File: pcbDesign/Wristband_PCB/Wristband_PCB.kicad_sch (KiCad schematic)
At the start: 5 parts, among them U1 module_adxl345, U2 SEN0344, U3 ESP32-C3_SUPERMINI_TH

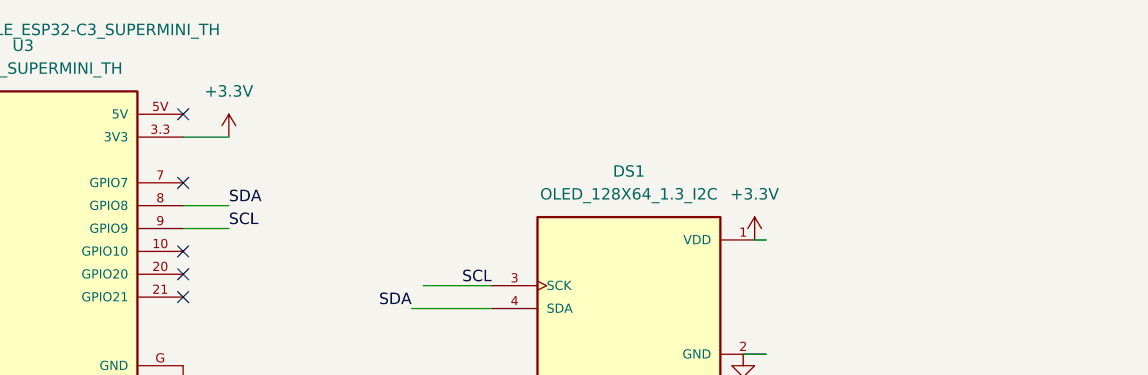
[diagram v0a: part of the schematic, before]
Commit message: added a power socket
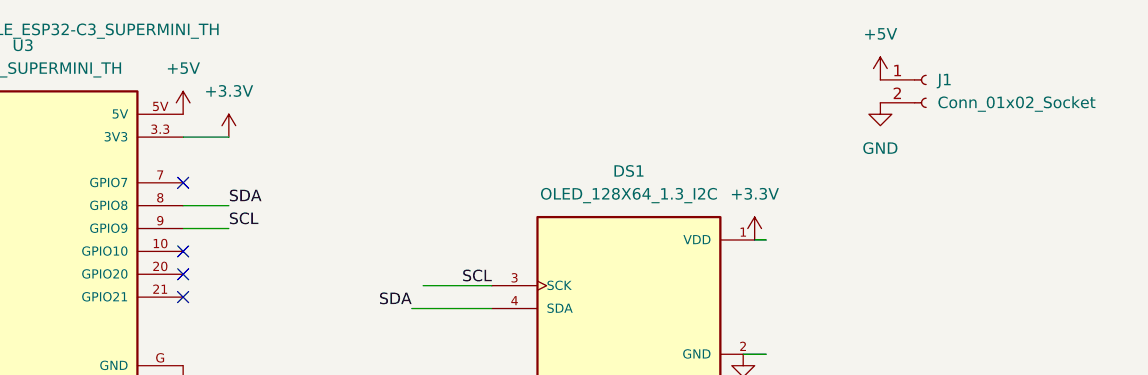
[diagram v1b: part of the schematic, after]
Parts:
- added J1: Conn_01x02_Socket, Connector_PinSocket_2.54mm:PinSocket_1x02_P2.54mm_Vertical, symbol Connector:Conn_01x02_Socket
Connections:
- net GND: now also J1.2 (Pin_2)
- net +5V: now reaches U3.5V
- net +5V: now also J1.1 (Pin_1)
- no-connect marks 22 -> 21
